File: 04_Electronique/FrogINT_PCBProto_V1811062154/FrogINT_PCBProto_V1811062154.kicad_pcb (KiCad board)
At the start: 2 copper layers, 100 x 100 mm, 34 parts, among them J1 USB_B_Mini, J2 Conn_01x01_Female, J3 AVR-JTAG-10, Q1 PMV48XP, Q2 PMV48XP, SW1 SW_SPST, SW2 SW_SPST, U1 NCP1117-5.0_SOT223, U2 LP2985-3.3, U3 ATmega16U4RC-AU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

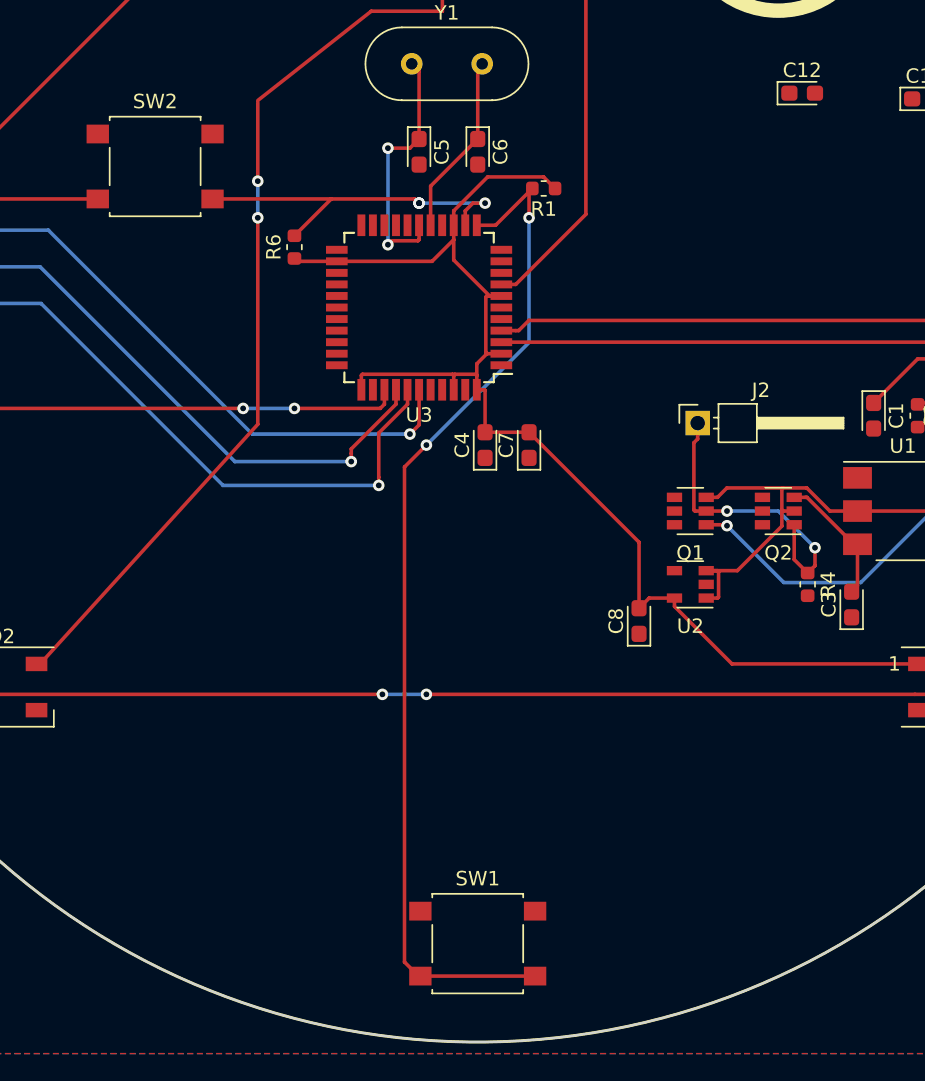
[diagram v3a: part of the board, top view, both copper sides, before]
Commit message: ***Commit du 14/01/2019 :
- Mise à jour des micro switch - choix d'une référence plus petites.
- Mise à jour des librairies
- Ajout des librairies SamacSys directement dans le projet
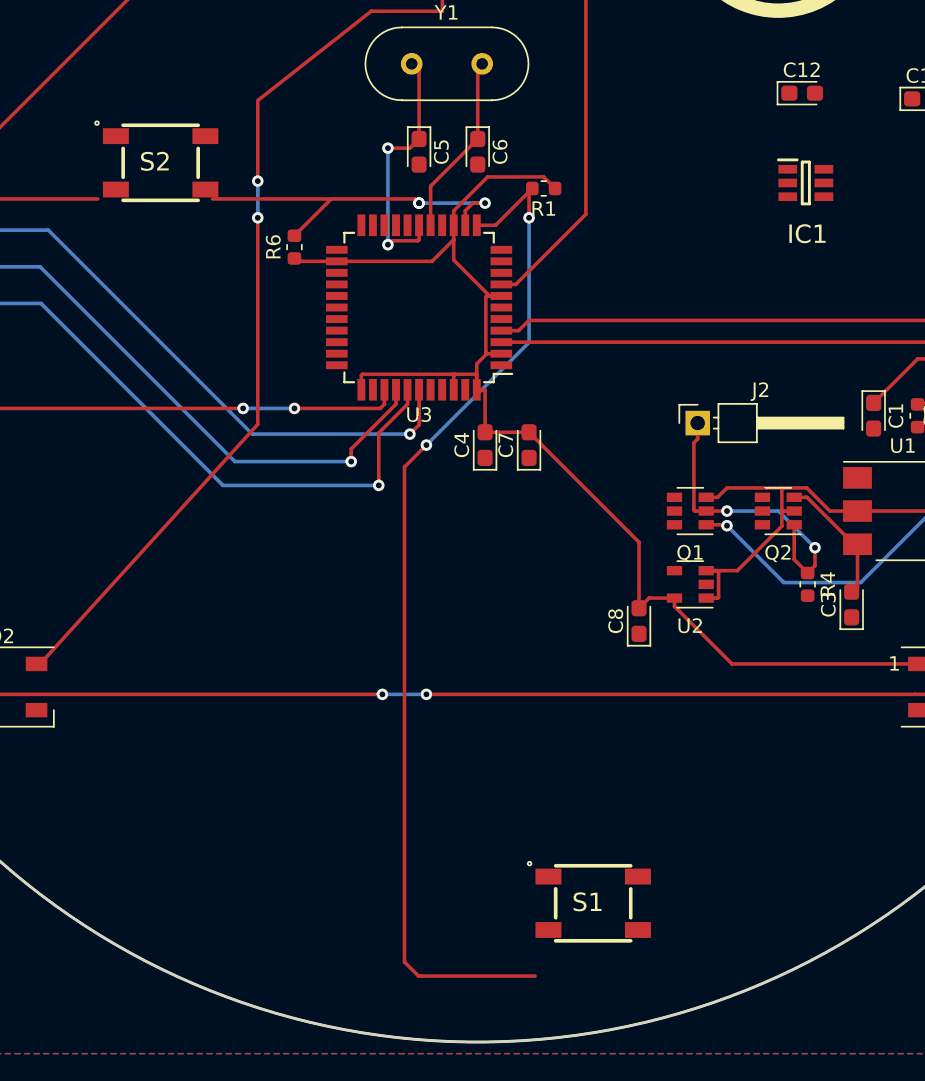
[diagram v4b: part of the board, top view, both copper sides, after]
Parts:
- removed SW1, SW2: SW_SPST, FTA_FrogINT_Library_Footprint_Package:SW_SPST_B3S-1000
- added IC1: TTP223-BA6, SamacSys_Parts:SOT95P285X126-6N, F.Cu at (169.3, 88.8)
- added S1: SKQGAKE010, SamacSys_Parts:SKQGAKE010, F.Cu at (154.6, 138.7)
- added S2: SKQGAKE010, SamacSys_Parts:SKQGAKE010, F.Cu at (124.6, 87.4)
